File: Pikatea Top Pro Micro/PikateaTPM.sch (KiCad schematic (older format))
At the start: 21 parts, among them J1 USB_B_Mini, J2 Conn_01x08, J3 Conn_01x08, J4 Conn_01x05, J6 AVR-ISP-6, J7 01x15, U1 ATmega32U4, X1 16MHz

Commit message: Replace usb mini footprint
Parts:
- J1: footprint Connector_USB:USB_Mini-B_AdamTech_MUSB-B5-S-VT-TSMT-1_SMD_Vertical -> usb_mini:USB-Mini-B_ LCSC-C46398
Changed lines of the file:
@@
 F 0 "J1" H 3707 3567 50  0000 C CNN
 F 1 "USB_B_Mini" H 3707 3476 50  0000 C CNN
-F 2 "Connector_USB:USB_Mini-B_AdamTech_MUSB-B5-S-VT-TSMT-1_SMD_Vertical" H 3800 3050 50  0001 C CNN
+F 2 "usb_mini:USB-Mini-B_ LCSC-C46398" H 3800 3050 50  0001 C CNN
 F 3 "~" H 3800 3050 50  0001 C CNN
 	1    3650 3100

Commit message: add BOM
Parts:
- J1: LCSC (none) -> C46398
- J6: symbol Connector:AVR-ISP-6 -> PikateaTPM-rescue:AVR-ISP-6-Connector
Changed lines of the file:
@@
 EESchema Schematic File Version 4
-LIBS:PikateaTPM-cache
-EELAYER 26 0
+EELAYER 30 0
 EELAYER END
 $Descr A4 11693 8268
@@
 F 2 "usb_mini:USB-Mini-B_ LCSC-C46398" H 3800 3050 50  0001 C CNN
 F 3 "~" H 3800 3050 50  0001 C CNN
+F 4 "C46398" H 3650 3100 50  0001 C CNN "LCSC"
 	1    3650 3100
 	1    0    0    -1
@@
 	4350 2900 4350 2750
 $Comp
-L Connector:AVR-ISP-6 J6
+L PikateaTPM-rescue:AVR-ISP-6-Connector J6
 U 1 1 5F129CF4
 P 5500 2800

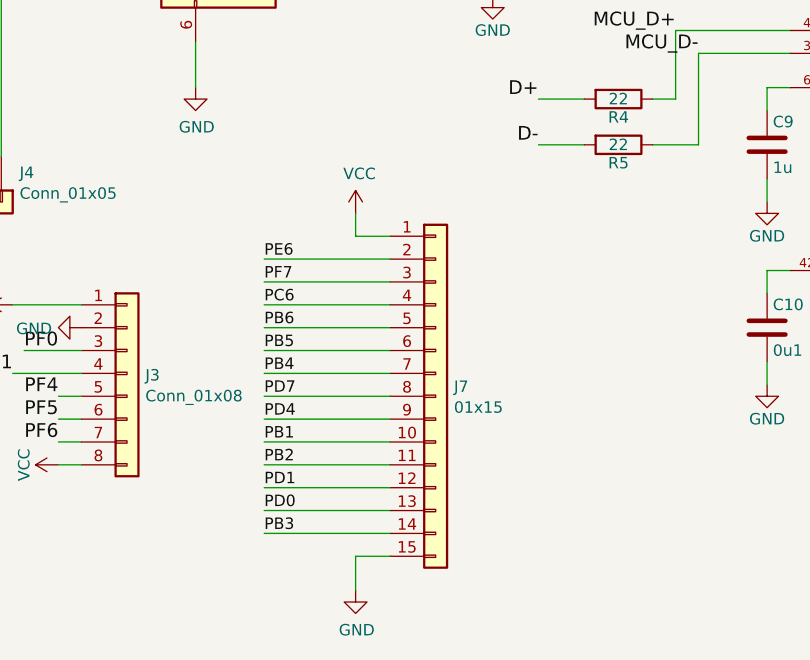
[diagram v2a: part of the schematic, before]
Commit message: Bottom Switch plate, footprints in place
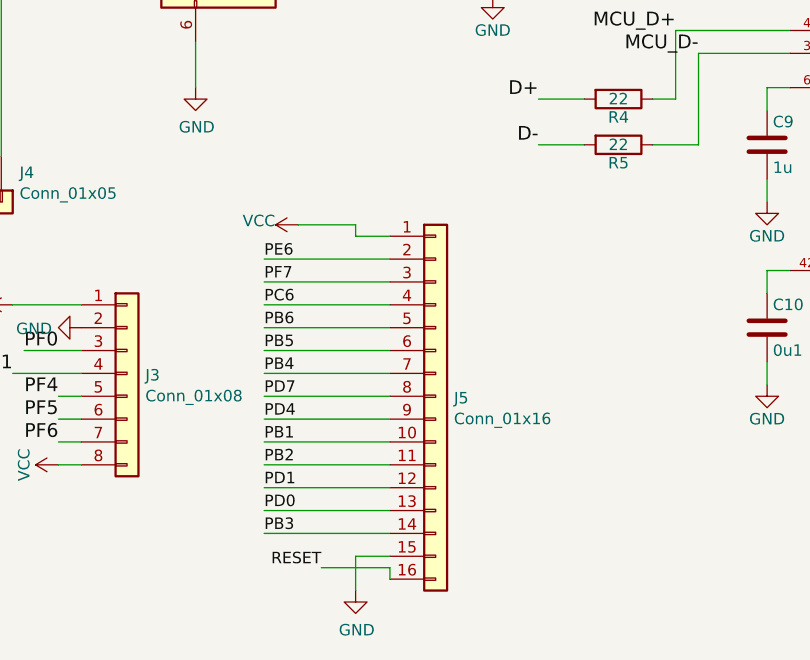
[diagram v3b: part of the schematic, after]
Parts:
- removed J7: 01x15, Connector_PinHeader_2.54mm:PinHeader_1x15_P2.54mm_Vertical, symbol Connector_Generic:Conn_01x15
- added J5: Conn_01x16, Connector_PinHeader_2.54mm:PinHeader_1x16_P2.54mm_Vertical, symbol Connector_Generic:Conn_01x16
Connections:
- net GND: now also J5.15 (Pin_15)
- net PB1: now also J5.10 (Pin_10)
- net PB2: now also J5.11 (Pin_11)
- net PB3: now also J5.14 (Pin_14)
- net PB4: now also J5.7 (Pin_7)
- net PB5: now also J5.6 (Pin_6)
- net PB6: now also J5.5 (Pin_5)
- net PC6: now also J5.4 (Pin_4)
- net PD0: now also J5.13 (Pin_13)
- net PD1: now also J5.12 (Pin_12)
- net PD4: now also J5.9 (Pin_9)
- net PD7: now also J5.8 (Pin_8)
- net PE6: now also J5.2 (Pin_2)
- net PF7: now also J5.3 (Pin_3)
- net RESET: now also J5.16 (Pin_16)
- net VBUS: now also J5.1 (Pin_1)
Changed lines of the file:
@@
 	5900 2600 6250 2600
-$Comp
-L Connector_Generic:Conn_01x15 J7
-U 1 1 5F1687DA
-P 6450 4750
-F 0 "J7" H 6530 4792 50  0000 L CNN
-F 1 "01x15" H 6530 4701 50  0000 L CNN
-F 2 "Connector_PinHeader_2.54mm:PinHeader_1x15_P2.54mm_Vertical" H 6450 4750 50  0001 C CNN
-F 3 "~" H 6450 4750 50  0001 C CNN
-	1    6450 4750
-	1    0    0    -1
-$EndComp
-$Comp
-L power:VCC #PWR0105
-U 1 1 5F16DE4C
-P 6100 3950
-F 0 "#PWR0105" H 6100 3800 50  0001 C CNN
-F 1 "VCC" H 6117 4123 50  0000 C CNN
-F 2 "" H 6100 3950 50  0001 C CNN
-F 3 "" H 6100 3950 50  0001 C CNN
-	1    6100 3950
-	1    0    0    -1
-$EndComp
 $Comp
 L power:GND #PWR0106
@@
 	6250 4050 6100 4050
 Wire Wire Line
-	6100 4050 6100 3950
+	6100 4050 6100 4000
 Text Label 5700 4450 0    50   ~ 0
 PB6
@@
 Wire Wire Line
 	3800 4650 3700 4650
+$Comp
+L Connector_Generic:Conn_01x16 J5
+U 1 1 5F10039A
+P 6450 4750
+F 0 "J5" H 6530 4742 50  0000 L CNN
+F 1 "Conn_01x16" H 6530 4651 50  0000 L CNN
+F 2 "Connector_PinHeader_2.54mm:PinHeader_1x16_P2.54mm_Vertical" H 6450 4750 50  0001 C CNN
+F 3 "~" H 6450 4750 50  0001 C CNN
+	1    6450 4750
+	1    0    0    -1
+$EndComp
+Wire Wire Line
+	6100 4000 5850 4000
+Wire Wire Line
+	6250 5500 5950 5500
+Wire Wire Line
+	6250 5550 6250 5500
+Text Label 5950 5500 2    50   ~ 0
+RESET
+$Comp
+L power:VCC #PWR0105
+U 1 1 5F16DE4C
+P 5850 4000
+F 0 "#PWR0105" H 5850 3850 50  0001 C CNN
+F 1 "VCC" V 5867 4173 50  0000 C CNN
+F 2 "" H 5850 4000 50  0001 C CNN
+F 3 "" H 5850 4000 50  0001 C CNN
+	1    5850 4000
+	0    -1   -1   0
+$EndComp
 $EndSCHEMATC

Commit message: Update to 0805 footprints
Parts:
- C1, C10, C2, C3, C4, C5, C6, C7, C8, C9: footprint Capacitor_SMD:C_0402_1005Metric -> Capacitor_SMD:C_0805_2012Metric
- R3, R4, R5: footprint Resistor_SMD:R_0402_1005Metric -> Resistor_SMD:R_0805_2012Metric
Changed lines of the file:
@@
 EESchema Schematic File Version 4
+LIBS:PikateaTPM-cache
 EELAYER 30 0
 EELAYER END
@@
 F 0 "R4" V 7330 3450 50  0000 C CNN
 F 1 "22" V 7250 3450 50  0000 C CNN
-F 2 "Resistor_SMD:R_0402_1005Metric" V 7180 3450 50  0001 C CNN
+F 2 "Resistor_SMD:R_0805_2012Metric" V 7180 3450 50  0001 C CNN
 F 3 "" H 7250 3450 50  0001 C CNN
 F 4 "C25092" V 7250 3450 50  0001 C CNN "LCSC"
@@
 F 0 "R5" V 7330 3650 50  0000 C CNN
 F 1 "22" V 7250 3650 50  0000 C CNN
-F 2 "Resistor_SMD:R_0402_1005Metric" V 7180 3650 50  0001 C CNN
+F 2 "Resistor_SMD:R_0805_2012Metric" V 7180 3650 50  0001 C CNN
 F 3 "" H 7250 3650 50  0001 C CNN
 F 4 "C25092" V 7250 3650 50  0001 C CNN "LCSC"
@@
 F 0 "C8" H 7075 2800 50  0000 L CNN
 F 1 "22p" H 7075 2600 50  0000 L CNN
-F 2 "Capacitor_SMD:C_0402_1005Metric" H 7088 2550 50  0001 C CNN
+F 2 "Capacitor_SMD:C_0805_2012Metric" H 7088 2550 50  0001 C CNN
 F 3 "" H 7050 2700 50  0001 C CNN
 F 4 "C1555" H 7050 2700 50  0001 C CNN "LCSC"
@@
 F 0 "C7" H 7075 2100 50  0000 L CNN
 F 1 "22p" H 7075 1900 50  0000 L CNN
-F 2 "Capacitor_SMD:C_0402_1005Metric" H 7088 1850 50  0001 C CNN
+F 2 "Capacitor_SMD:C_0805_2012Metric" H 7088 1850 50  0001 C CNN
 F 3 "" H 7050 2000 50  0001 C CNN
 F 4 "C1555" H 7050 2000 50  0001 C CNN "LCSC"
@@
 F 0 "R3" V 7730 1600 50  0000 C CNN
 F 1 "10k" V 7650 1600 50  0000 C CNN
-F 2 "Resistor_SMD:R_0402_1005Metric" V 7580 1600 50  0001 C CNN
+F 2 "Resistor_SMD:R_0805_2012Metric" V 7580 1600 50  0001 C CNN
 F 3 "" H 7650 1600 50  0001 C CNN
 F 4 "C25744" V 7650 1600 50  0001 C CNN "LCSC"
@@
 F 0 "C9" H 7925 3750 50  0000 L CNN
 F 1 "1u" H 7925 3550 50  0000 L CNN
-F 2 "Capacitor_SMD:C_0402_1005Metric" H 7938 3500 50  0001 C CNN
+F 2 "Capacitor_SMD:C_0805_2012Metric" H 7938 3500 50  0001 C CNN
 F 3 "" H 7900 3650 50  0001 C CNN
 F 4 "C52923" H 7900 3650 50  0001 C CNN "LCSC"
@@
 F 0 "C10" H 7925 4550 50  0000 L CNN
 F 1 "0u1" H 7925 4350 50  0000 L CNN
-F 2 "Capacitor_SMD:C_0402_1005Metric" H 7938 4300 50  0001 C CNN
+F 2 "Capacitor_SMD:C_0805_2012Metric" H 7938 4300 50  0001 C CNN
 F 3 "" H 7900 4450 50  0001 C CNN
 F 4 "C1525" H 7900 4450 50  0001 C CNN "LCSC"
@@
 F 0 "C1" H 5125 1250 50  0000 L CNN
 F 1 "0u1" H 5125 1050 50  0000 L CNN
-F 2 "Capacitor_SMD:C_0402_1005Metric" H 5138 1000 50  0001 C CNN
+F 2 "Capacitor_SMD:C_0805_2012Metric" H 5138 1000 50  0001 C CNN
 F 3 "" H 5100 1150 50  0001 C CNN
 F 4 "C1525" H 5100 1150 50  0001 C CNN "LCSC"
@@
 F 0 "C2" H 5425 1250 50  0000 L CNN
 F 1 "0u1" H 5425 1050 50  0000 L CNN
-F 2 "Capacitor_SMD:C_0402_1005Metric" H 5438 1000 50  0001 C CNN
+F 2 "Capacitor_SMD:C_0805_2012Metric" H 5438 1000 50  0001 C CNN
 F 3 "" H 5400 1150 50  0001 C CNN
 F 4 "C1525" H 5400 1150 50  0001 C CNN "LCSC"
@@
 F 0 "C3" H 5725 1250 50  0000 L CNN
 F 1 "0u1" H 5725 1050 50  0000 L CNN
-F 2 "Capacitor_SMD:C_0402_1005Metric" H 5738 1000 50  0001 C CNN
+F 2 "Capacitor_SMD:C_0805_2012Metric" H 5738 1000 50  0001 C CNN
 F 3 "" H 5700 1150 50  0001 C CNN
 F 4 "C1525" H 5700 1150 50  0001 C CNN "LCSC"
@@
 F 0 "C4" H 6025 1250 50  0000 L CNN
 F 1 "0u1" H 6025 1050 50  0000 L CNN
-F 2 "Capacitor_SMD:C_0402_1005Metric" H 6038 1000 50  0001 C CNN
+F 2 "Capacitor_SMD:C_0805_2012Metric" H 6038 1000 50  0001 C CNN
 F 3 "" H 6000 1150 50  0001 C CNN
 F 4 "C1525" H 6000 1150 50  0001 C CNN "LCSC"
@@
 F 0 "C6" H 6625 1250 50  0000 L CNN
 F 1 "4u7" H 6625 1050 50  0000 L CNN
-F 2 "Capacitor_SMD:C_0402_1005Metric" H 6638 1000 50  0001 C CNN
+F 2 "Capacitor_SMD:C_0805_2012Metric" H 6638 1000 50  0001 C CNN
 F 3 "" H 6600 1150 50  0001 C CNN
 F 4 "C23733" H 6600 1150 50  0001 C CNN "LCSC"
@@
 F 0 "C5" H 6325 1250 50  0000 L CNN
 F 1 "0u1" H 6325 1050 50  0000 L CNN
-F 2 "Capacitor_SMD:C_0402_1005Metric" H 6338 1000 50  0001 C CNN
+F 2 "Capacitor_SMD:C_0805_2012Metric" H 6338 1000 50  0001 C CNN
 F 3 "" H 6300 1150 50  0001 C CNN
 F 4 "C1525" H 6300 1150 50  0001 C CNN "LCSC"

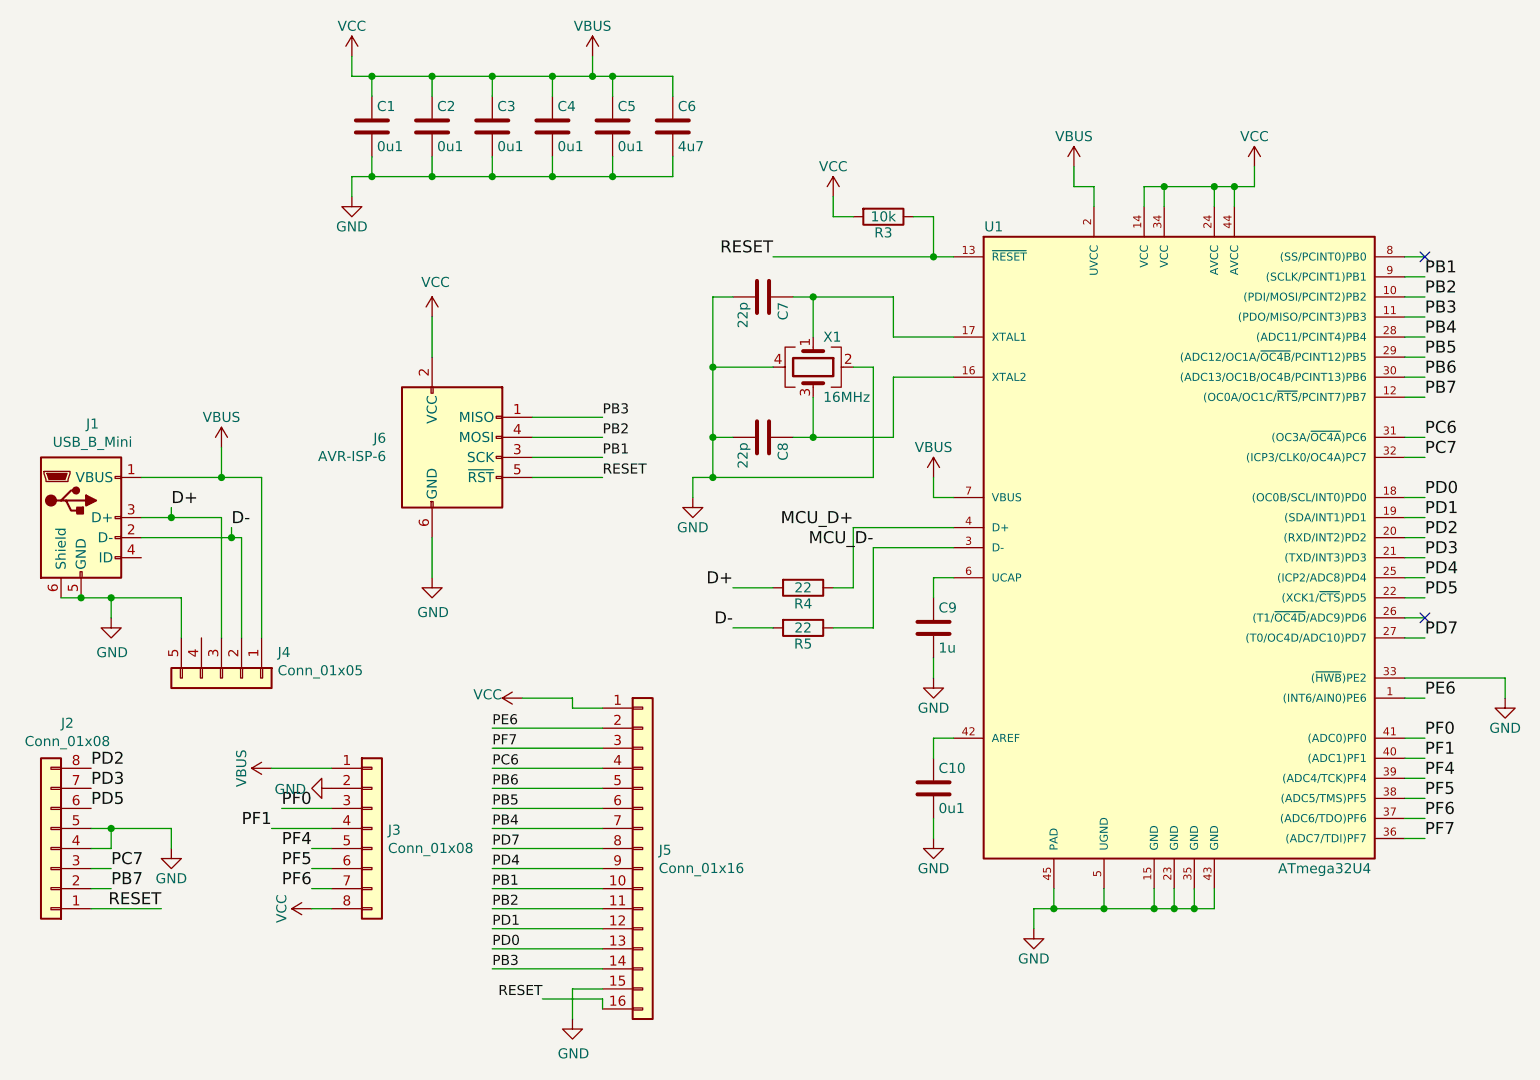
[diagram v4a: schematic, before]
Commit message: manually meged 0805 branch to master
I hate myself for doing this
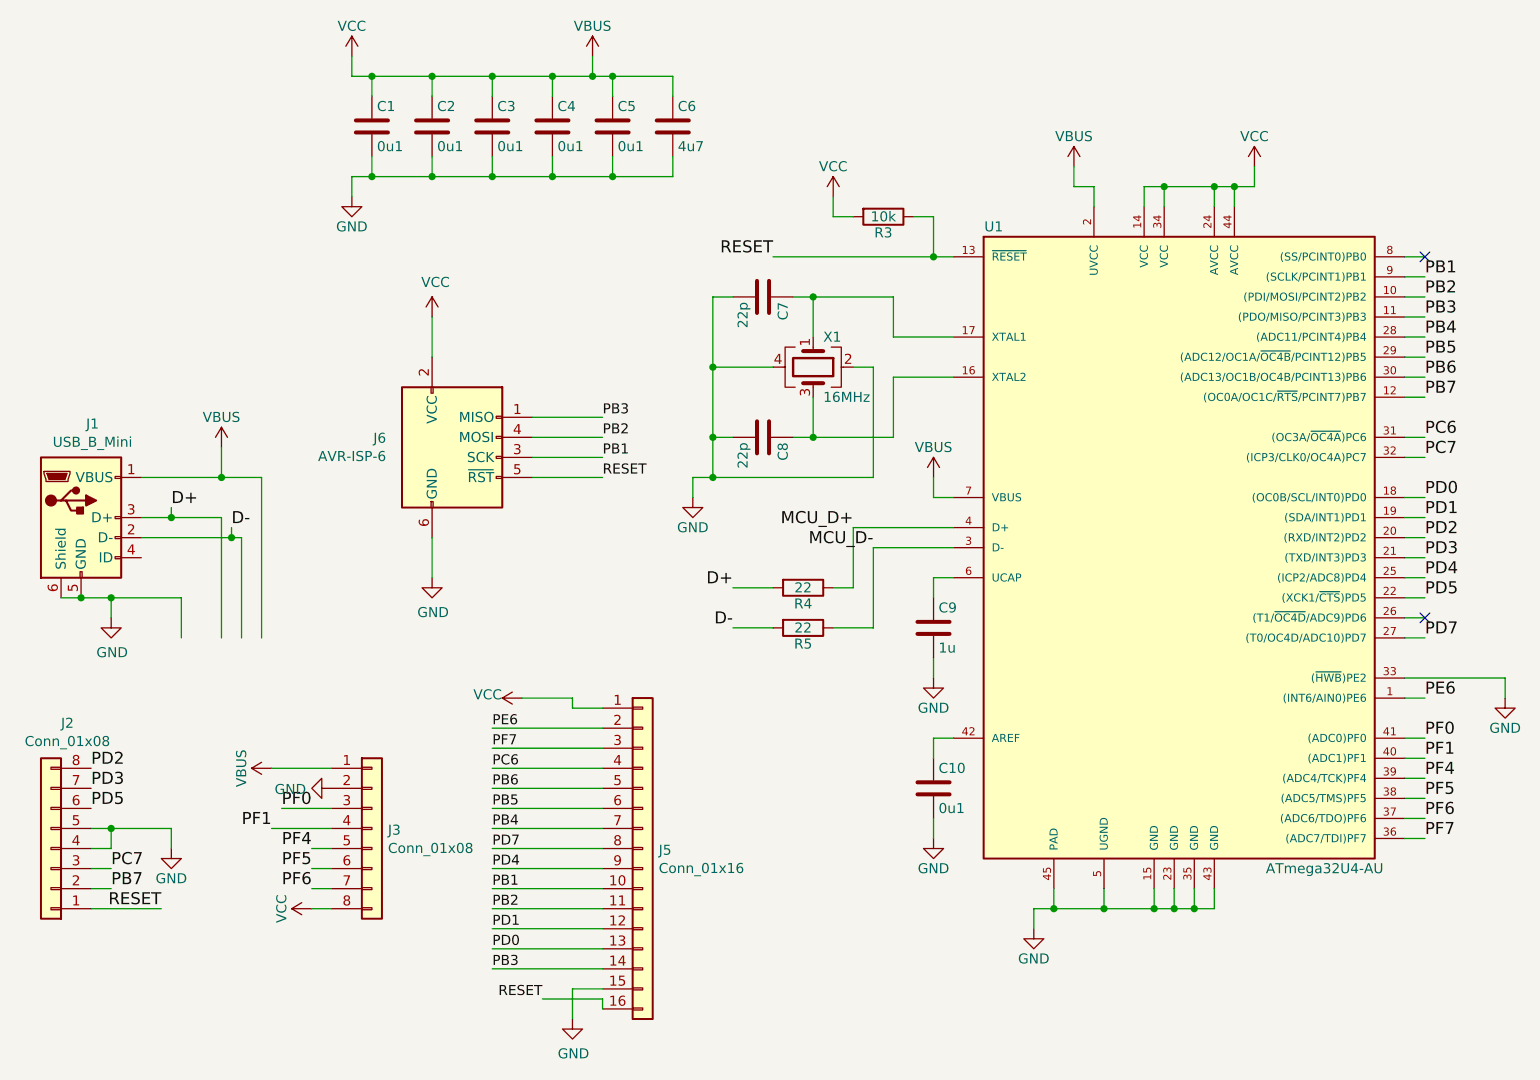
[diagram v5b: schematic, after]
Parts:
- removed J4: Conn_01x05, Connector_PinHeader_2.54mm:PinHeader_1x05_P2.54mm_Vertical, symbol Connector_Generic:Conn_01x05
- U1: value ATmega32U4 -> ATmega32U4-AU
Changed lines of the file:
@@
 EESchema Schematic File Version 4
-LIBS:PikateaTPM-cache
 EELAYER 30 0
 EELAYER END
@@
 P 9150 3350
 F 0 "U1" H 8200 5050 50  0000 C CNN
-F 1 "ATmega32U4" H 9850 1850 50  0000 C CNN
+F 1 "ATmega32U4-AU" H 9850 1850 50  0000 C CNN
 F 2 "Package_QFP:TQFP-44_10x10mm_P0.8mm" H 9150 3350 50  0001 C CIN
 F 3 "" H 10250 4450 50  0001 C CNN
 F 4 "C44854" H 9150 3350 50  0001 C CNN "LCSC"
+F 5 "" H 9150 3350 50  0001 C CNN "Digikey"
 	1    9150 3350
 	1    0    0    -1
@@
 Connection ~ 6200 900
 Connection ~ 6000 900
-$Comp
-L Connector_Generic:Conn_01x05 J4
-U 1 1 5F025D8D
-P 4350 3900
-F 0 "J4" V 4222 4180 50  0000 L CNN
-F 1 "Conn_01x05" V 4313 4180 50  0000 L CNN
-F 2 "Connector_PinHeader_2.54mm:PinHeader_1x05_P2.54mm_Vertical" H 4350 3900 50  0001 C CNN
-F 3 "~" H 4350 3900 50  0001 C CNN
-	1    4350 3900
-	0    1    1    0
-$EndComp
 Wire Wire Line
 	3800 3500 4150 3500
-Wire Wire Line
-	4150 3500 4150 3700
 Connection ~ 3800 3500
 Wire Wire Line
 	4350 2900 4550 2900
-Wire Wire Line
-	4550 2900 4550 3700
 Connection ~ 4350 2900
 Wire Wire Line
-	4450 3200 4450 3700
-Wire Wire Line
 	3950 3100 4100 3100
 Wire Wire Line
 	3950 3200 4400 3200
-Wire Wire Line
-	4350 3100 4350 3700
 Wire Wire Line
 	4400 3150 4400 3200
@@
 	0    -1   -1   0
 $EndComp
+Wire Wire Line
+	4150 3500 4150 3700
+Wire Wire Line
+	4550 2900 4550 3700
+Wire Wire Line
+	4450 3200 4450 3700
+Wire Wire Line
+	4350 3100 4350 3700
 $EndSCHEMATC
